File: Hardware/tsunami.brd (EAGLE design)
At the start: 74.9 x 73.7 mm, 158 parts, among them J1 VDC-IN, J10 TRIG2, J11 TRIG1, J12 USD-SDIO-SOCKET, J13 GND, J14 AUDIO I/O, J15 MIDI, J2 GND-IN, J3 DEBUG, J4 USB-MICROB", J5 CORTEX_DEBUGPTH, J6 3.3VA, J7 3.3V, J8 PLAYING, J9 FTDI_DEVICE, Q1 2.5A/30V, U1 LM1117, U2 LM1117, U3 ATSAMS70N20A-AN, U4 AK4618VQ, U5 74AHC1G125, U6 6N138M, Y1 11.2896 MHz

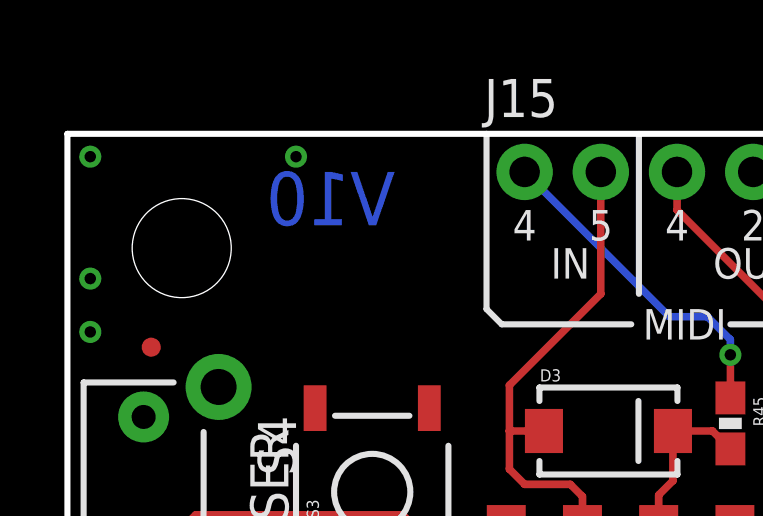
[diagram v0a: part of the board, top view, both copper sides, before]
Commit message: Fixing silkscreen labels on panel.
Transposed 2 and 5 labels on MIDI out port.
Rolled version to V11 on all files.
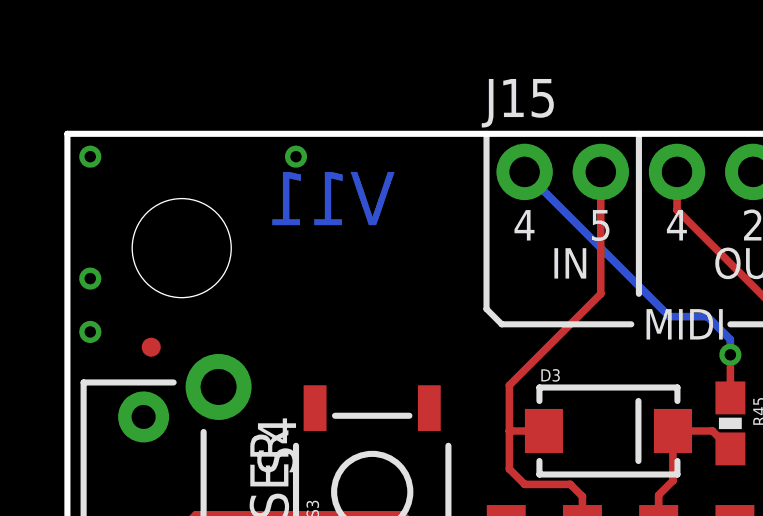
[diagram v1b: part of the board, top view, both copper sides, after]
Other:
- board text added: "V11"
- board text removed: "V10"
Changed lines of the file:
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@@
 <wire x1="0" y1="73.66" x2="0" y2="0" width="0.2032" layer="20"/>
 <text x="29.21" y="-31.75" size="1.778" layer="51" font="vector" ratio="10">Jamie Robertson &amp; Byron Jacquot</text>
-<text x="10.922" y="70.612" size="1.778" layer="16" font="vector" ratio="15" rot="MR0">V10</text>
+<text x="10.922" y="70.612" size="1.778" layer="16" font="vector" ratio="15" rot="MR0">V11</text>
 <text x="38.608" y="68.58" size="3.81" layer="21" font="vector" ratio="15" align="bottom-center">Tsunami</text>
 <text x="38.1" y="66.548" size="1.4224" layer="21" font="vector" ratio="15" align="bottom-center">Super WAV Trigger</text>
